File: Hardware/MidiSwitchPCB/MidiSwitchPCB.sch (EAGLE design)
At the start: 74 parts, among them IC3 74LVC2G04GW,125, K1 APF30212C, K2 APF30212C, K3 APF30212C, K4 APF30212C, K5 APF30212C, K6 APF30212C, K7 APF30212C, K8 APF30212C, Q1 BSS123, Q2 BSS123, Q3 BSS123, Q4 BSS123, Q5 BSS123, Q6 BSS123, Q7 BSS123, Q8 BSS123, X1 1503_09, X2 1503_09, X3 1503_09, X4 1503_09

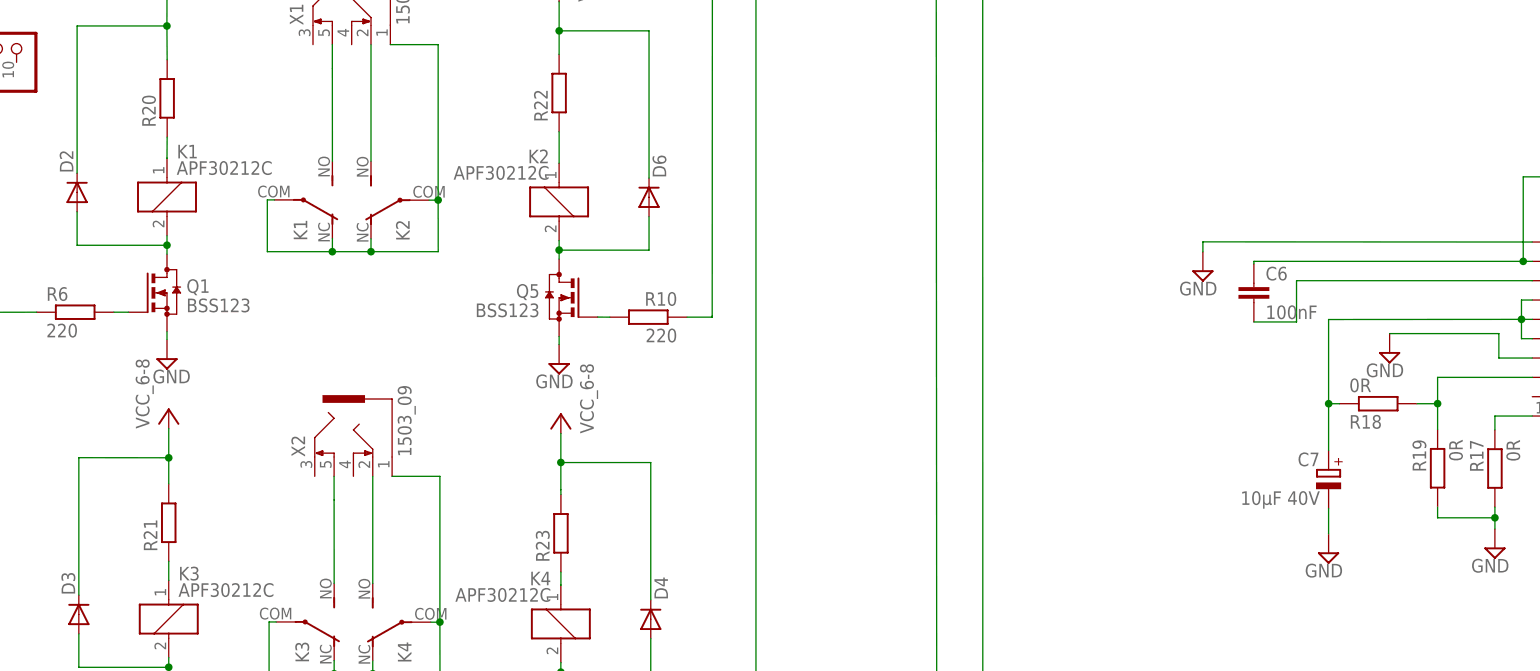
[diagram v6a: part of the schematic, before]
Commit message: changed some device packages
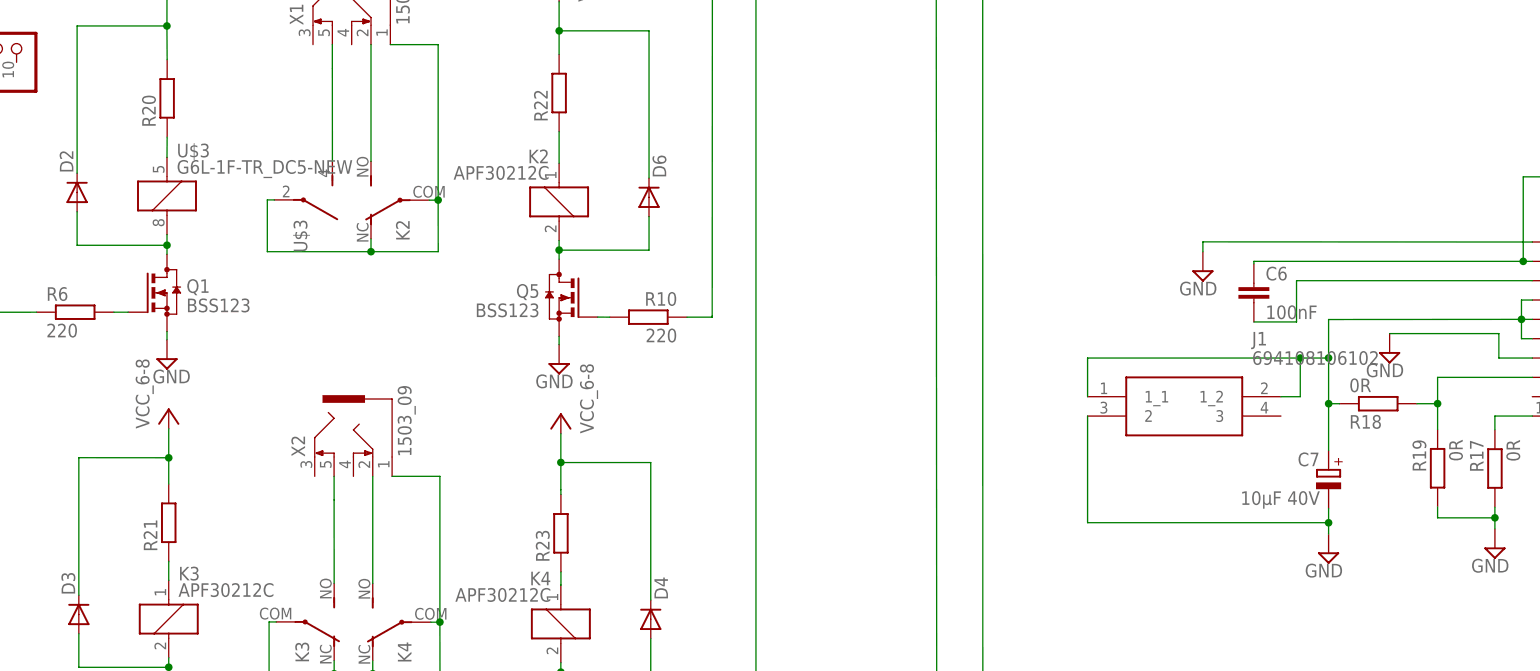
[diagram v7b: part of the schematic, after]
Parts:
- removed K1: APF30212C, relay:APF30212C
- added J1: 694108106102, SamacSys_Parts:694108106102
- added U$3: G6L-1F-TR_DC5-NEW, SamacSys_Parts:G6L-1F-TR_DC5-NEW
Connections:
- removed net N$53: C7.+, PS1.IGN, PS1.VINL, PS1.VINP, R18.1
- new net N$67: C7.+, J1.1_1, PS1.IGN, PS1.VINL, PS1.VINP, R18.1
- net GND: now also J1.2
- net N$12: now also U$3G$1.2; no longer K11.2
- net N$36: now also U$3G$2.S; no longer K12.S
- net N$38: now also U$3G$2.P; no longer K12.O, K12.P
- net N$59: now also U$3G$1.1; no longer K11.1
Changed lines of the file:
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@@
 <part name="CN8" library="pinhead" deviceset="PINHD-1X6" device=""/>
 <part name="CN5" library="pinhead" deviceset="PINHD-1X10" device=""/>
-<part name="K1" library="relay" deviceset="APF30212C" device=""/>
 <part name="Q1" library="transistor-small-signal" deviceset="BSS123" device=""/>
 <part name="P+3" library="supply1" deviceset="VCC" device="" value="VCC_6-8"/>
@@
 <part name="R26" library="rcl" deviceset="R-EU_" device="R0603"/>
 <part name="R27" library="rcl" deviceset="R-EU_" device="R0603"/>
+<part name="J1" library="SamacSys_Parts" deviceset="694108106102" device=""/>
+<part name="U$3" library="SamacSys_Parts" deviceset="G6L-1F-TR_DC5-NEW" device=""/>
 </parts>
 <sheets>
@@
 <instance part="CN8" gate="A" x="479.85" y="75.43" rot="R180"/>
 <instance part="CN5" gate="A" x="143.79" y="94.73" rot="R90"/>
-<instance part="K1" gate="1" x="176.25" y="74.49"/>
-<instance part="K1" gate="2" x="192.9" y="74.11" rot="R270"/>
 <instance part="Q1" gate="G$1" x="176.25" y="61.9"/>
 <instance part="P+3" gate="VCC" x="176.25" y="103.31"/>
@@
 <instance part="R26" gate="G$1" x="177.08" y="-82.09" rot="R90"/>
 <instance part="R27" gate="G$1" x="228.62" y="-82.62" rot="R90"/>
+<instance part="J1" gate="G$1" x="297.18" y="48.26"/>
+<instance part="U$3" gate="G$1" x="176.25" y="74.63"/>
+<instance part="U$3" gate="G$2" x="190.36" y="74.11" rot="R270"/>
 </instances>
 <busses>
@@
 <pinref part="C7" gate="G$1" pin="-"/>
 <pinref part="SUPPLY17" gate="GND" pin="GND"/>
-<wire x1="328.84" y1="30.24" x2="328.84" y2="33.57" width="0.1524" layer="91"/>
+<wire x1="328.84" y1="30.24" x2="328.84" y2="31.7" width="0.1524" layer="91"/>
+<pinref part="J1" gate="G$1" pin="2"/>
+<wire x1="328.84" y1="31.7" x2="328.84" y2="31.71" width="0.1524" layer="91"/>
+<wire x1="328.84" y1="31.71" x2="328.84" y2="33.57" width="0.1524" layer="91"/>
+<wire x1="297.18" y1="45.72" x2="297.18" y2="31.71" width="0.1524" layer="91"/>
+<wire x1="297.18" y1="31.71" x2="328.84" y2="31.71" width="0.1524" layer="91"/>
+<junction x="328.84" y="31.7"/>
 </segment>
 <segment>
@@
 <net name="N$12" class="0">
 <segment>
-<pinref part="K1" gate="1" pin="2"/>
 <pinref part="Q1" gate="G$1" pin="D"/>
-<wire x1="176.25" y1="69.41" x2="176.25" y2="68.16" width="0.1524" layer="91"/>
 <pinref part="D2" gate="G$1" pin="A"/>
+<wire x1="176.25" y1="69.55" x2="176.25" y2="68.16" width="0.1524" layer="91"/>
 <wire x1="176.25" y1="68.16" x2="176.25" y2="68.15" width="0.1524" layer="91"/>
 <wire x1="176.25" y1="68.15" x2="176.25" y2="66.98" width="0.1524" layer="91"/>
@@
 <wire x1="164.44" y1="68.15" x2="164.44" y2="72.55" width="0.1524" layer="91"/>
 <junction x="176.25" y="68.16"/>
+<pinref part="U$3" gate="G$1" pin="2"/>
 </segment>
 </net>
@@
 <segment>
 <pinref part="X1" gate="G$1" pin="5"/>
-<pinref part="K1" gate="2" pin="S"/>
 <wire x1="197.97" y1="94.51" x2="197.97" y2="91.41" width="0.1524" layer="91"/>
 <wire x1="197.97" y1="91.41" x2="197.98" y2="79.19" width="0.1524" layer="91"/>
+<pinref part="U$3" gate="G$2" pin="S"/>
 </segment>
 </net>
@@
 <net name="N$38" class="0">
 <segment>
-<pinref part="K1" gate="2" pin="P"/>
 <wire x1="190.36" y1="74.11" x2="189.43" y2="74.11" width="0.1524" layer="91"/>
 <wire x1="189.43" y1="74.11" x2="189.43" y2="67.31" width="0.1524" layer="91"/>
-<wire x1="189.43" y1="67.31" x2="197.97" y2="67.31" width="0.1524" layer="91"/>
+<wire x1="189.43" y1="67.31" x2="203.05" y2="67.31" width="0.1524" layer="91"/>
 <pinref part="K2" gate="2" pin="P"/>
-<wire x1="197.97" y1="67.31" x2="197.98" y2="67.31" width="0.1524" layer="91"/>
-<wire x1="197.98" y1="67.31" x2="203.05" y2="67.31" width="0.1524" layer="91"/>
 <wire x1="203.05" y1="67.31" x2="211.88" y2="67.31" width="0.1524" layer="91"/>
 <wire x1="211.88" y1="67.31" x2="211.87" y2="74.08" width="0.1524" layer="91"/>
@@
 <pinref part="K2" gate="2" pin="O"/>
 <wire x1="203.05" y1="69" x2="203.05" y2="67.31" width="0.1524" layer="91"/>
-<pinref part="K1" gate="2" pin="O"/>
-<wire x1="197.98" y1="69.03" x2="197.98" y2="67.31" width="0.1524" layer="91"/>
-<junction x="197.97" y="67.31"/>
 <junction x="203.05" y="67.31"/>
 <junction x="211.87" y="74.09"/>
+<pinref part="U$3" gate="G$2" pin="P"/>
 </segment>
 </net>
@@
 <pinref part="PS1" gate="G$1" pin="BST1"/>
 <wire x1="355.6" y1="63.5" x2="324.63" y2="63.5" width="0.1524" layer="91"/>
-</segment>
-</net>
-<net name="N$53" class="0">
-<segment>
-<pinref part="PS1" gate="G$1" pin="VINP"/>
-<wire x1="355.6" y1="60.96" x2="354.18" y2="60.96" width="0.1524" layer="91"/>
-<wire x1="354.18" y1="58.42" x2="328.84" y2="58.4" width="0.1524" layer="91"/>
-<pinref part="C7" gate="G$1" pin="+"/>
-<wire x1="328.84" y1="58.4" x2="328.84" y2="47.34" width="0.1524" layer="91"/>
-<wire x1="328.84" y1="47.34" x2="328.84" y2="41.19" width="0.1524" layer="91"/>
-<wire x1="354.18" y1="60.96" x2="354.18" y2="58.42" width="0.1524" layer="91"/>
-<pinref part="PS1" gate="G$1" pin="IGN"/>
-<wire x1="354.18" y1="58.42" x2="354.18" y2="55.88" width="0.1524" layer="91"/>
-<wire x1="354.18" y1="55.88" x2="355.6" y2="55.88" width="0.1524" layer="91"/>
-<pinref part="PS1" gate="G$1" pin="VINL"/>
-<wire x1="355.6" y1="58.42" x2="354.18" y2="58.42" width="0.1524" layer="91"/>
-<junction x="354.18" y="58.42"/>
-<pinref part="R18" gate="G$1" pin="1"/>
-<wire x1="330.28" y1="47.34" x2="328.85" y2="47.34" width="0.1524" layer="91"/>
-<junction x="328.85" y="47.34"/>
-<wire x1="328.85" y1="47.34" x2="328.84" y2="47.34" width="0.1524" layer="91"/>
 </segment>
 </net>
@@
 <net name="N$59" class="0">
 <segment>
-<pinref part="K1" gate="1" pin="1"/>
 <pinref part="R20" gate="G$1" pin="1"/>
-<wire x1="176.25" y1="79.57" x2="176.25" y2="79.6" width="0.1524" layer="91"/>
-<wire x1="176.25" y1="79.6" x2="176.27" y2="82.37" width="0.1524" layer="91"/>
+<wire x1="176.25" y1="79.71" x2="176.27" y2="82.37" width="0.1524" layer="91"/>
+<pinref part="U$3" gate="G$1" pin="1"/>
 </segment>
 </net>
@@
 </segment>
 </net>
+<net name="N$67" class="0">
+<segment>
+<pinref part="J1" gate="G$1" pin="1_1"/>
+<wire x1="297.18" y1="48.26" x2="297.18" y2="53.34" width="0.1524" layer="91"/>
+<wire x1="297.18" y1="53.34" x2="325.12" y2="53.34" width="0.1524" layer="91"/>
+<wire x1="325.12" y1="53.34" x2="325.12" y2="48.26" width="0.1524" layer="91"/>
+<wire x1="325.12" y1="48.26" x2="322.59" y2="48.26" width="0.1524" layer="91"/>
+<pinref part="PS1" gate="G$1" pin="VINP"/>
+<wire x1="355.6" y1="60.96" x2="354.18" y2="60.96" width="0.1524" layer="91"/>
+<wire x1="354.18" y1="58.42" x2="328.84" y2="58.4" width="0.1524" layer="91"/>
+<pinref part="C7" gate="G$1" pin="+"/>
+<wire x1="328.84" y1="58.4" x2="328.84" y2="53.35" width="0.1524" layer="91"/>
+<wire x1="328.84" y1="53.35" x2="328.84" y2="53.34" width="0.1524" layer="91"/>
+<wire x1="328.84" y1="53.34" x2="328.84" y2="47.34" width="0.1524" layer="91"/>
+<wire x1="328.84" y1="47.34" x2="328.84" y2="41.19" width="0.1524" layer="91"/>
+<wire x1="354.18" y1="60.96" x2="354.18" y2="58.42" width="0.1524" layer="91"/>
+<pinref part="PS1" gate="G$1" pin="IGN"/>
+<wire x1="354.18" y1="58.42" x2="354.18" y2="55.88" width="0.1524" layer="91"/>
+<wire x1="354.18" y1="55.88" x2="355.6" y2="55.88" width="0.1524" layer="91"/>
+<pinref part="PS1" gate="G$1" pin="VINL"/>
+<wire x1="355.6" y1="58.42" x2="354.18" y2="58.42" width="0.1524" layer="91"/>
+<junction x="354.18" y="58.42"/>
+<pinref part="R18" gate="G$1" pin="1"/>
+<wire x1="330.28" y1="47.34" x2="328.85" y2="47.34" width="0.1524" layer="91"/>
+<junction x="328.85" y="47.34"/>
+<wire x1="328.85" y1="47.34" x2="328.84" y2="47.34" width="0.1524" layer="91"/>
+<wire x1="325.12" y1="53.34" x2="325.13" y2="53.34" width="0.1524" layer="91"/>
+<junction x="328.84" y="53.35"/>
+<junction x="325.13" y="53.34"/>
+<wire x1="325.13" y1="53.34" x2="328.84" y2="53.34" width="0.1524" layer="91"/>
+</segment>
+</net>

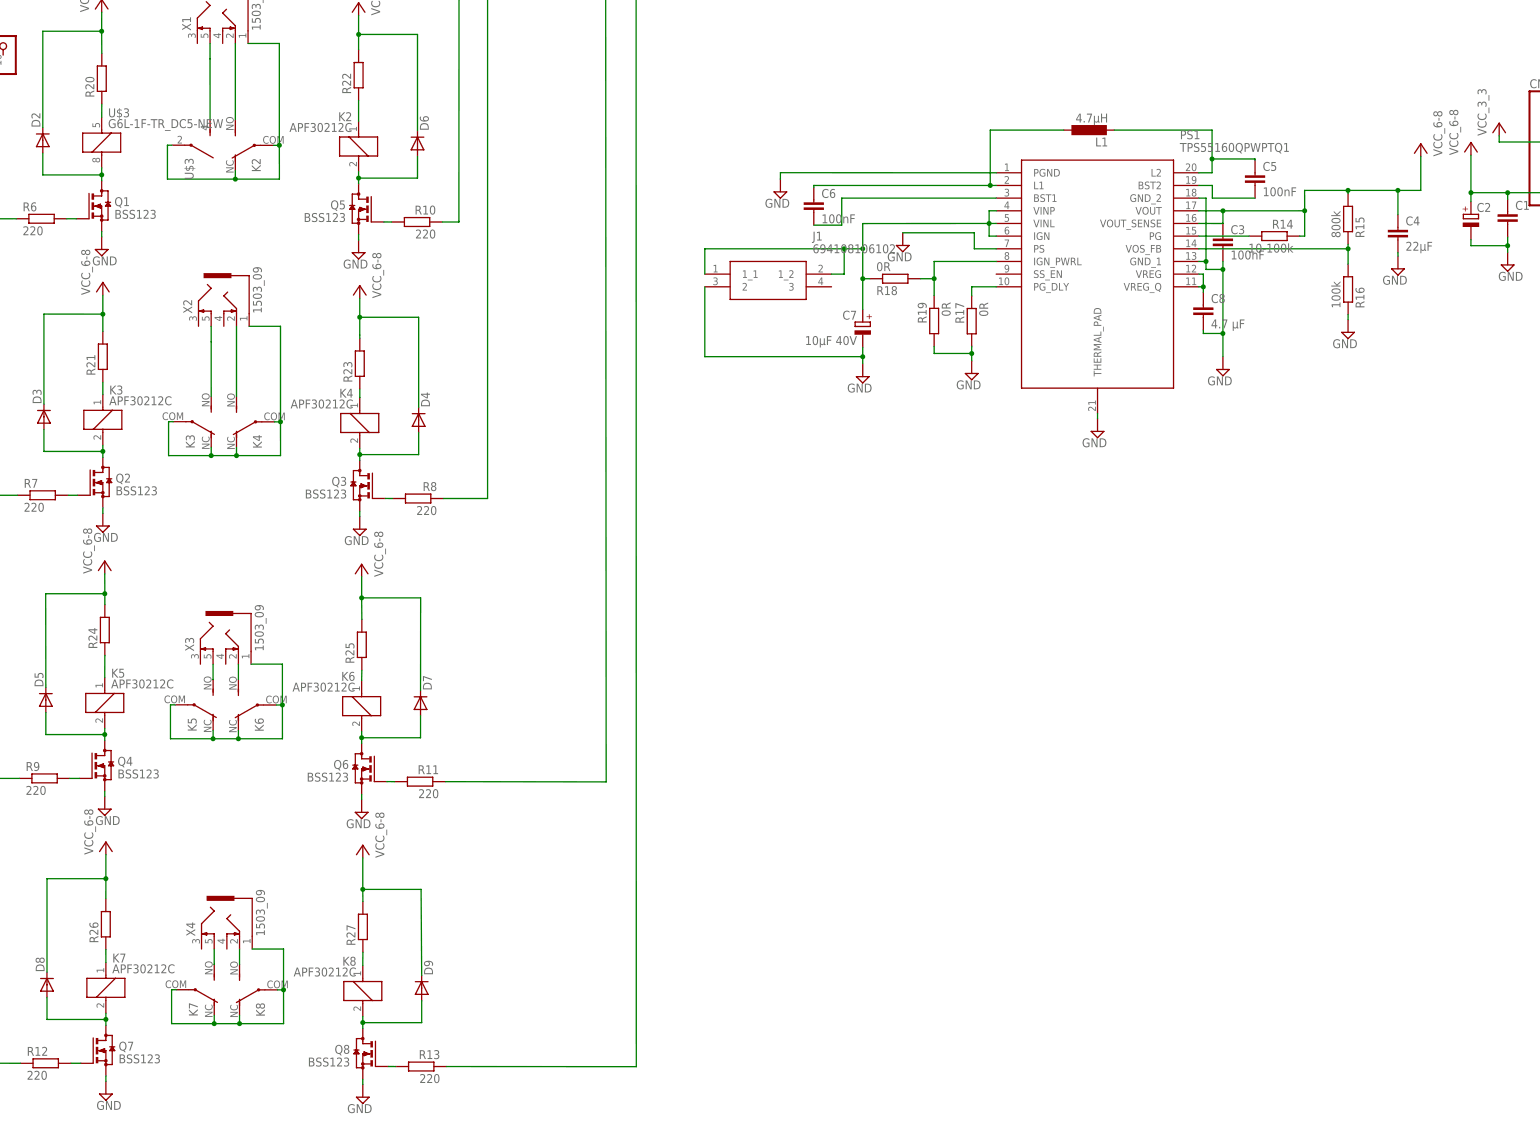
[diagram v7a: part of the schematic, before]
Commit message: placed devices on the layout
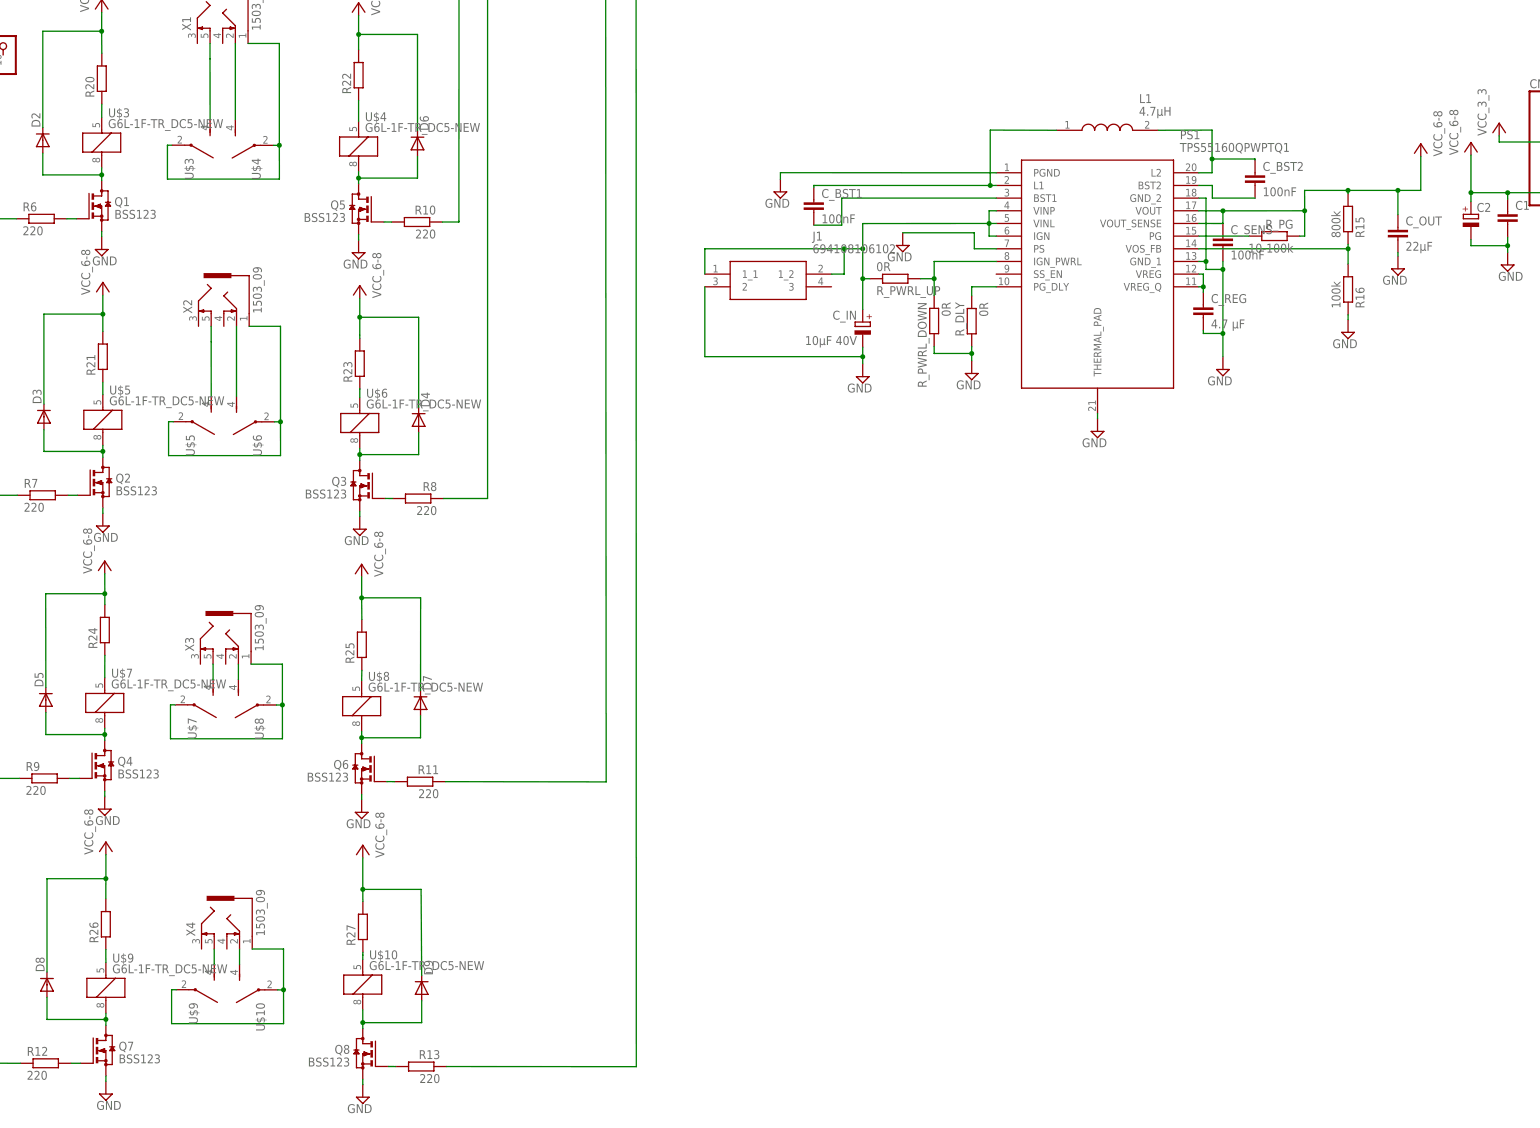
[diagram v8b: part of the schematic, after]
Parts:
- removed K2, K3, K4, K5, K6, K7, K8: APF30212C, relay:APF30212C
- added U$10, U$4, U$5, U$6, U$7, U$8, U$9: G6L-1F-TR_DC5-NEW, SamacSys_Parts:G6L-1F-TR_DC5-NEW
- L1: device rcl:L-EUWE-TPC -> NRS8030T4R7MJGJ:NRS8030T4R7MJGJ
- renumbered C3 to C_SENS, C4 to C_OUT, C5 to C_BST2, C6 to C_BST1, C7 to C_IN, C8 to C_REG, R14 to R_PG, R17 to R_DLY, R18 to R_PWRL_UP, R19 to R_PWRL_DOWN
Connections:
- removed net N$50: R15.1
- removed net N$66: K81.1, R27.1
- new net N$53: R23.1, U$6G$1.1
- net N$13: now also U$5G$1.2; no longer K31.2
- net N$16: now also U$6G$1.2; no longer K41.2
- net N$19: now also U$5G$2.S; no longer K32.S
- net N$20: now also U$4G$1.2; no longer K21.2
- net N$22: now also U$6G$2.S; no longer K42.S
- net N$23: now also U$5G$2.P, U$6G$2.P; no longer K32.O, K32.P, K42.O, K42.P
- net N$24: now also U$7G$1.2; no longer K51.2
- net N$26: now also U$8G$1.2; no longer K61.2
- net N$29: now also U$7G$2.S; no longer K52.S
- net N$30: now also U$8G$2.S; no longer K62.S
- net N$32: now also U$7G$2.P, U$8G$2.P; no longer K52.O, K52.P, K62.O, K62.P
- net N$33: now also U$9G$1.2; no longer K71.2
- net N$35: now also U$10G$1.2; no longer K81.2
- net N$37: now also U$4G$2.S; no longer K22.S
- net N$38: now also U$4G$2.P; no longer K22.O, K22.P
- net N$41: now also U$9G$2.S; no longer K72.S
- net N$42: now also U$10G$2.S; no longer K82.S
- net N$43: now also U$10G$2.P, U$9G$2.P; no longer K72.O, K72.P, K82.O, K82.P
- net N$49: now also R15.1
- net N$60: now also U$4G$1.1; no longer K21.1
- net N$61: now also U$5G$1.1; no longer K31.1
- net N$62: now also R27.1, U$10G$1.1; no longer K41.1, R23.1
- net N$63: now also U$7G$1.1; no longer K51.1
- net N$64: now also U$8G$1.1; no longer K61.1
- net N$65: now also U$9G$1.1; no longer K71.1
